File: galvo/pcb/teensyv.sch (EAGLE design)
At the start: 46 parts, among them IC1 RB-0512D, IC10 MCP4922-E/P, IC2.5 MAX6102, IC3 QUAD_OPAMPP, IC5 MAX6105, IC9 QUAD_OPAMPP

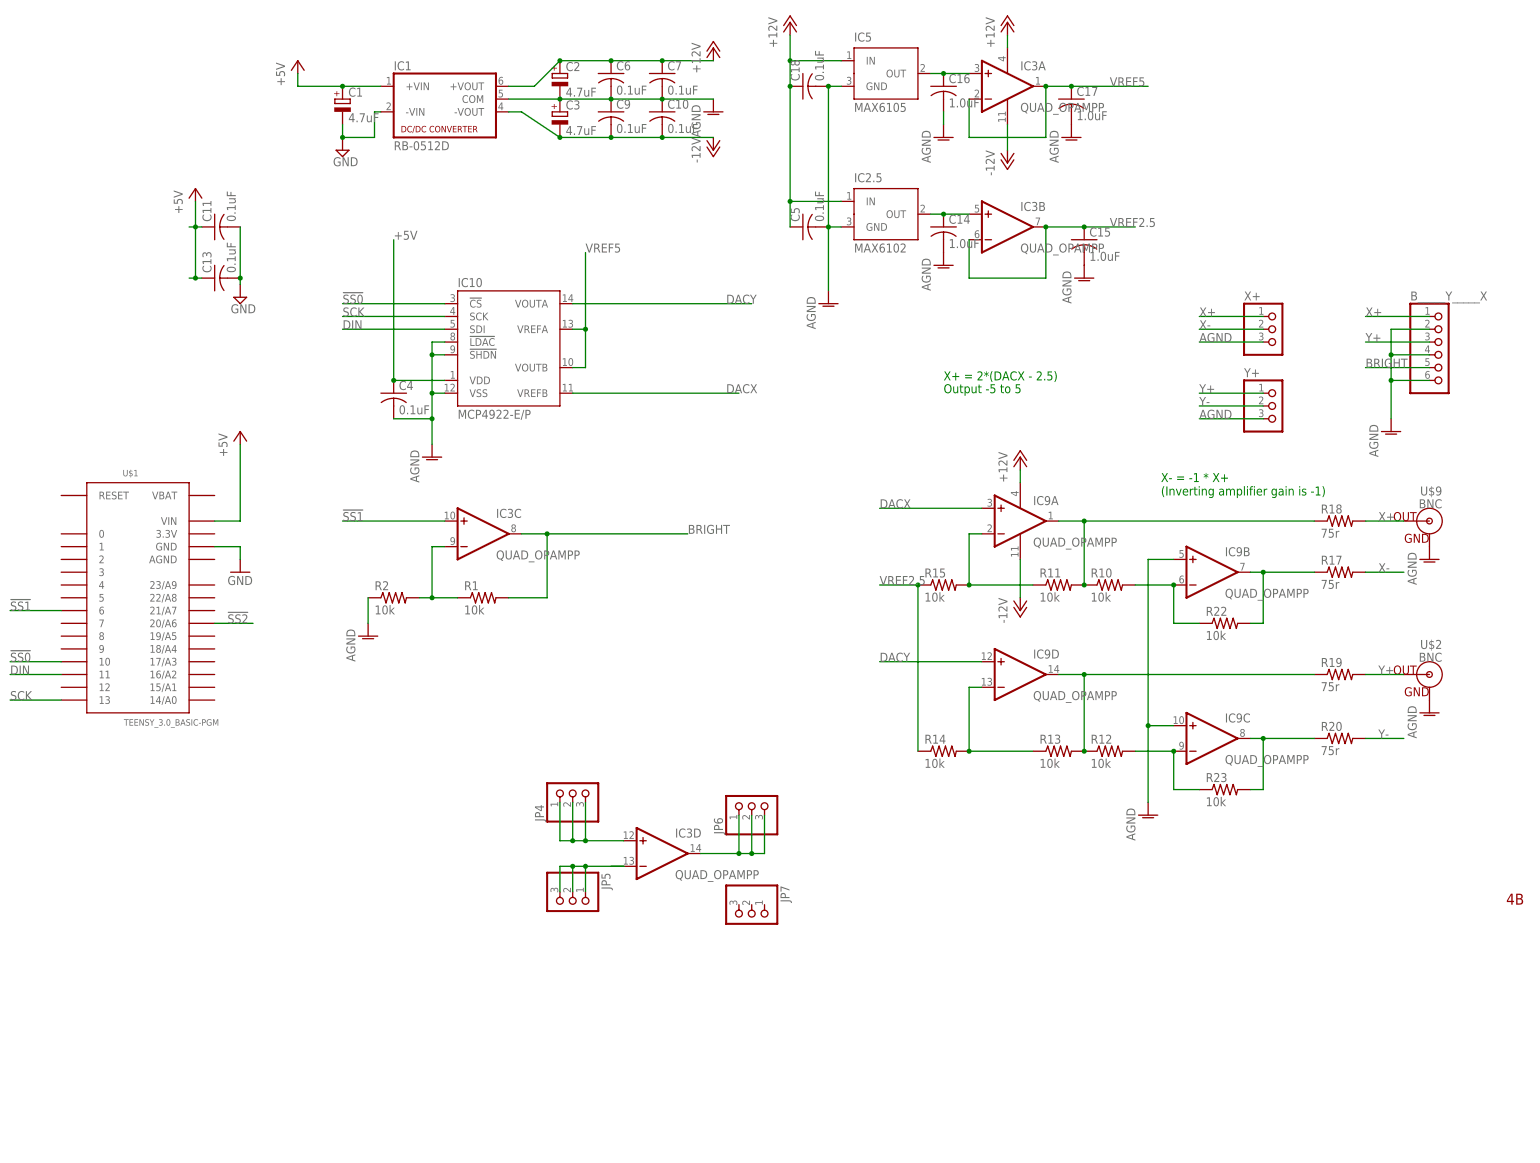
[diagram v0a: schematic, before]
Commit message: added LEDs and extra header
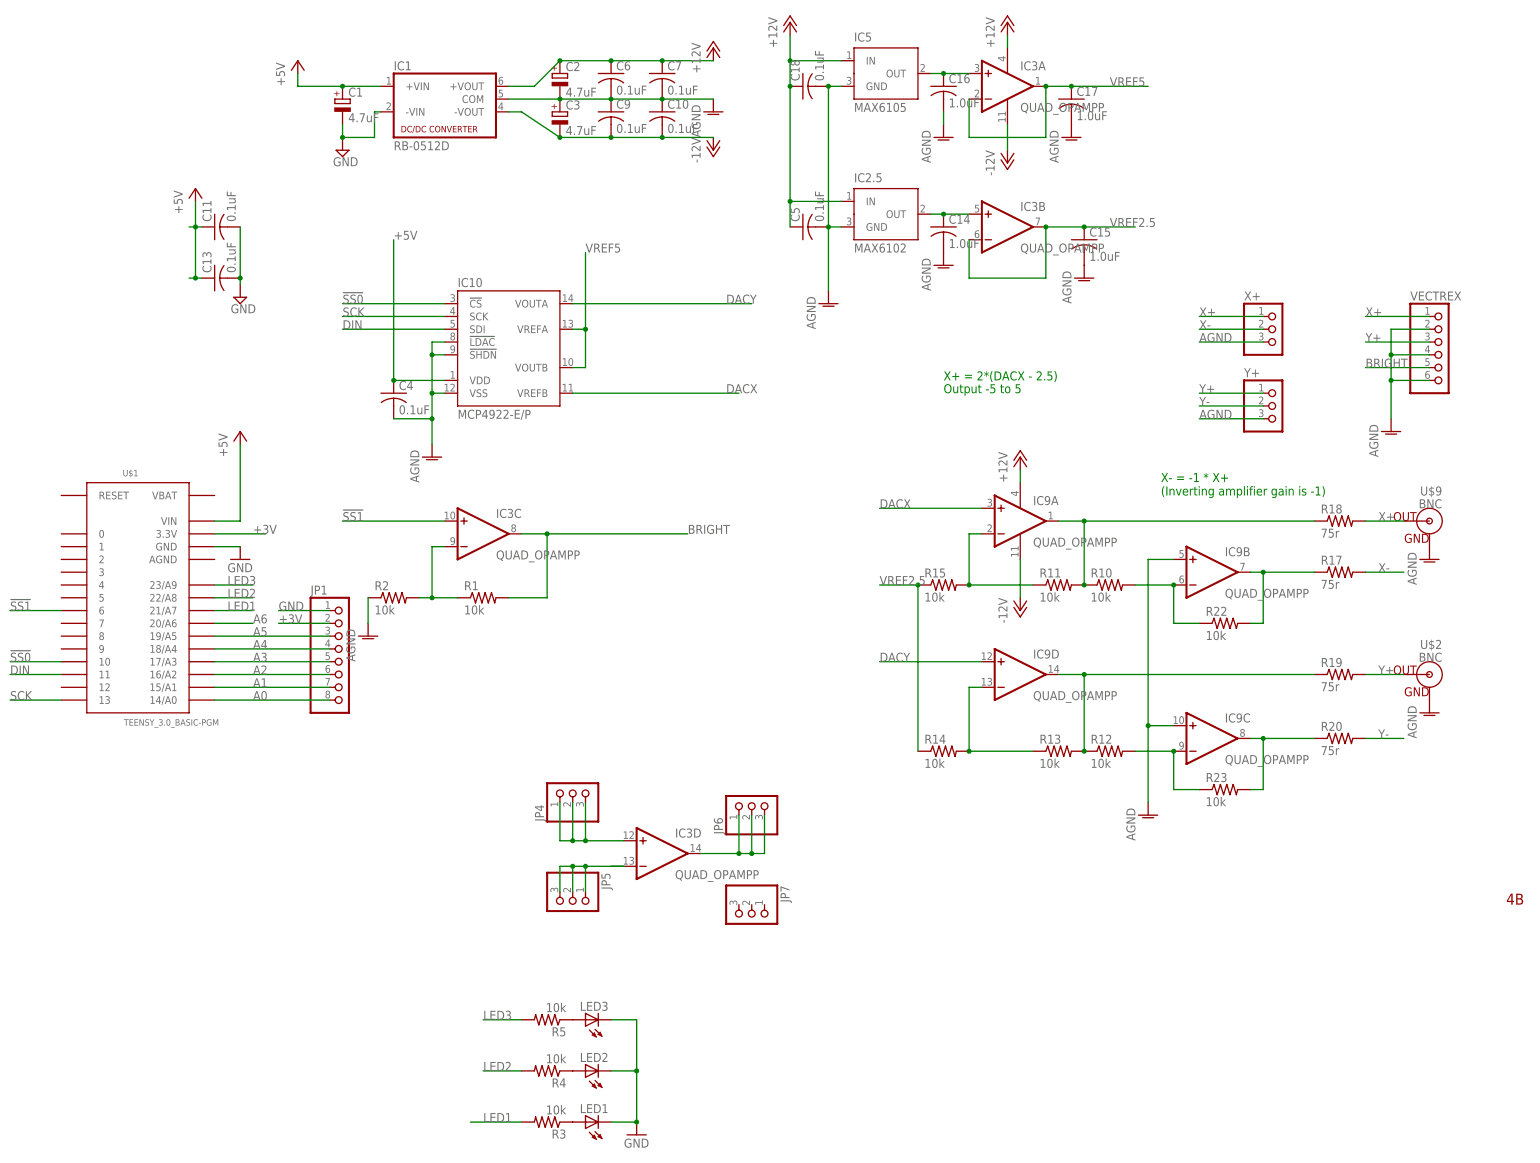
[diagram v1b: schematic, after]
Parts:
- added JP1: (no value), adafruit:PINHD-1X8CLEANBIG
- added LED1, LED2, LED3: (no value), adafruit:LED5MM
- added R3, R4, R5: 10k, adafruit:R-US_0204/2V
- renumbered B_____Y_____X to VECTREX
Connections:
- net !SS2 renamed A6
- new net +3V: JP1.2, U$1.3.3V
- new net A0: JP1.8, U$1.14/A0
- new net A1: JP1.7, U$1.15/A1
- new net A2: JP1.6, U$1.16/A2
- new net A3: JP1.5, U$1.17/A3
- new net A4: JP1.4, U$1.18/A4
- new net A5: JP1.3, U$1.19/A5
- new net LED1: R3.2, U$1.21/A7
- new net LED2: R4.2, U$1.22/A8
- new net LED3: R5.2, U$1.23/A9
- new net N$11: LED2.A, R4.1
- new net N$12: LED3.A, R5.1
- new net N$7: LED1.A, R3.1
- net GND: now also JP1.1, LED1.C, LED2.C, LED3.C
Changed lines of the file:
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@@
 <part name="AGND1" library="supply1" deviceset="AGND" device=""/>
 <part name="AGND2" library="supply1" deviceset="AGND" device=""/>
-<part name="B_____Y_____X" library="adafruit" deviceset="PINHD-1X6" device=""/>
+<part name="VECTREX" library="adafruit" deviceset="PINHD-1X6" device=""/>
 <part name="AGND4" library="supply1" deviceset="AGND" device=""/>
 <part name="X+" library="adafruit" deviceset="PINHD-1X3" device=""/>
@@
 <part name="JP6" library="adafruit" deviceset="PINHD-1X3" device=""/>
 <part name="JP7" library="adafruit" deviceset="PINHD-1X3" device=""/>
+<part name="LED1" library="adafruit" deviceset="LED" device="5MM"/>
+<part name="LED2" library="adafruit" deviceset="LED" device="5MM"/>
+<part name="LED3" library="adafruit" deviceset="LED" device="5MM"/>
+<part name="R3" library="adafruit" deviceset="R-US_" device="0204/2V" value="10k"/>
+<part name="R4" library="adafruit" deviceset="R-US_" device="0204/2V" value="10k"/>
+<part name="R5" library="adafruit" deviceset="R-US_" device="0204/2V" value="10k"/>
+<part name="GND1" library="supply1" deviceset="GND" device=""/>
+<part name="JP1" library="adafruit" deviceset="PINHD-1X8" device="CLEANBIG"/>
 </parts>
 <sheets>
@@
 <instance part="U$1" gate="G$1" x="-33.02" y="68.58"/>
 <instance part="P+2" gate="1" x="-12.7" y="101.6"/>
-<instance part="GND4" gate="1" x="-12.7" y="73.66"/>
+<instance part="GND4" gate="1" x="-12.7" y="76.2"/>
 <instance part="IC3" gate="A" x="139.7" y="170.18"/>
 <instance part="IC3" gate="B" x="139.7" y="142.24"/>
@@
 <instance part="AGND1" gate="VR1" x="223.52" y="76.2"/>
 <instance part="AGND2" gate="VR1" x="223.52" y="45.72"/>
-<instance part="B_____Y_____X" gate="A" x="226.06" y="116.84"/>
+<instance part="VECTREX" gate="A" x="226.06" y="116.84"/>
 <instance part="AGND4" gate="VR1" x="215.9" y="101.6"/>
 <instance part="X+" gate="A" x="193.04" y="121.92"/>
@@
 <instance part="JP6" gate="A" x="88.9" y="27.94" rot="R90"/>
 <instance part="JP7" gate="A" x="88.9" y="5.08" rot="R270"/>
+<instance part="LED1" gate="G$1" x="55.88" y="-35.56" rot="R90"/>
+<instance part="LED2" gate="G$1" x="55.88" y="-25.4" rot="R90"/>
+<instance part="LED3" gate="G$1" x="55.88" y="-15.24" rot="R90"/>
+<instance part="R3" gate="G$1" x="48.26" y="-35.56" rot="R180"/>
+<instance part="R4" gate="G$1" x="48.26" y="-25.4" rot="R180"/>
+<instance part="R5" gate="G$1" x="48.26" y="-15.24" rot="R180"/>
+<instance part="GND1" gate="1" x="66.04" y="-38.1"/>
+<instance part="JP1" gate="G$1" x="7.62" y="58.42"/>
 </instances>
 <busses>
@@
 <pinref part="U$1" gate="G$1" pin="GND"/>
 <wire x1="-17.78" y1="78.74" x2="-12.7" y2="78.74" width="0.1524" layer="91"/>
-<wire x1="-12.7" y1="78.74" x2="-12.7" y2="76.2" width="0.1524" layer="91"/>
 <pinref part="GND4" gate="1" pin="GND"/>
+</segment>
+<segment>
+<pinref part="LED1" gate="G$1" pin="C"/>
+<wire x1="60.96" y1="-35.56" x2="66.04" y2="-35.56" width="0.1524" layer="91"/>
+<wire x1="66.04" y1="-35.56" x2="66.04" y2="-25.4" width="0.1524" layer="91"/>
+<pinref part="LED3" gate="G$1" pin="C"/>
+<wire x1="66.04" y1="-25.4" x2="66.04" y2="-15.24" width="0.1524" layer="91"/>
+<wire x1="66.04" y1="-15.24" x2="60.96" y2="-15.24" width="0.1524" layer="91"/>
+<pinref part="LED2" gate="G$1" pin="C"/>
+<wire x1="60.96" y1="-25.4" x2="66.04" y2="-25.4" width="0.1524" layer="91"/>
+<junction x="66.04" y="-25.4"/>
+<pinref part="GND1" gate="1" pin="GND"/>
+<junction x="66.04" y="-35.56"/>
+</segment>
+<segment>
+<pinref part="JP1" gate="G$1" pin="1"/>
+<wire x1="5.08" y1="66.04" x2="-5.08" y2="66.04" width="0.1524" layer="91"/>
+<label x="-5.08" y="66.04" size="1.778" layer="95"/>
 </segment>
 </net>
@@
 </segment>
 <segment>
-<pinref part="B_____Y_____X" gate="A" pin="1"/>
+<pinref part="VECTREX" gate="A" pin="1"/>
 <wire x1="223.52" y1="124.46" x2="210.82" y2="124.46" width="0.1524" layer="91"/>
 <label x="210.82" y="124.46" size="1.778" layer="95"/>
@@
 </segment>
 <segment>
-<pinref part="B_____Y_____X" gate="A" pin="3"/>
+<pinref part="VECTREX" gate="A" pin="3"/>
 <wire x1="223.52" y1="119.38" x2="210.82" y2="119.38" width="0.1524" layer="91"/>
 <label x="210.82" y="119.38" size="1.778" layer="95"/>
@@
 </segment>
 </net>
-<net name="!SS2" class="0">
+<net name="A6" class="0">
 <segment>
 <pinref part="U$1" gate="G$1" pin="20/A6"/>
 <wire x1="-17.78" y1="63.5" x2="-10.16" y2="63.5" width="0.1524" layer="91"/>
-<label x="-15.24" y="63.5" size="1.778" layer="95"/>
+<label x="-10.16" y="63.5" size="1.778" layer="95"/>
 </segment>
 </net>
@@
 </segment>
 <segment>
-<pinref part="B_____Y_____X" gate="A" pin="5"/>
+<pinref part="VECTREX" gate="A" pin="5"/>
 <wire x1="223.52" y1="114.3" x2="210.82" y2="114.3" width="0.1524" layer="91"/>
 <label x="210.82" y="114.3" size="1.778" layer="95"/>
@@
 </segment>
 <segment>
-<pinref part="B_____Y_____X" gate="A" pin="4"/>
+<pinref part="VECTREX" gate="A" pin="4"/>
 <wire x1="223.52" y1="116.84" x2="215.9" y2="116.84" width="0.1524" layer="91"/>
 <wire x1="215.9" y1="116.84" x2="215.9" y2="111.76" width="0.1524" layer="91"/>
-<pinref part="B_____Y_____X" gate="A" pin="6"/>
+<pinref part="VECTREX" gate="A" pin="6"/>
 <wire x1="215.9" y1="111.76" x2="215.9" y2="104.14" width="0.1524" layer="91"/>
 <wire x1="223.52" y1="111.76" x2="215.9" y2="111.76" width="0.1524" layer="91"/>
-<pinref part="B_____Y_____X" gate="A" pin="2"/>
+<pinref part="VECTREX" gate="A" pin="2"/>
 <wire x1="223.52" y1="121.92" x2="215.9" y2="121.92" width="0.1524" layer="91"/>
 <wire x1="215.9" y1="121.92" x2="215.9" y2="116.84" width="0.1524" layer="91"/>
@@
 </segment>
 </net>
+<net name="N$7" class="0">
+<segment>
+<pinref part="LED1" gate="G$1" pin="A"/>
+<pinref part="R3" gate="G$1" pin="1"/>
+</segment>
+</net>
+<net name="N$11" class="0">
+<segment>
+<pinref part="LED2" gate="G$1" pin="A"/>
+<pinref part="R4" gate="G$1" pin="1"/>
+</segment>
+</net>
+<net name="N$12" class="0">
+<segment>
+<pinref part="LED3" gate="G$1" pin="A"/>
+<pinref part="R5" gate="G$1" pin="1"/>
+</segment>
+</net>
+<net name="LED3" class="0">
+<segment>
+<pinref part="R5" gate="G$1" pin="2"/>
+<wire x1="43.18" y1="-15.24" x2="35.56" y2="-15.24" width="0.1524" layer="91"/>
+<label x="35.56" y="-15.24" size="1.778" layer="95"/>
+</segment>
+<segment>
+<pinref part="U$1" gate="G$1" pin="23/A9"/>
+<wire x1="-17.78" y1="71.12" x2="-10.16" y2="71.12" width="0.1524" layer="91"/>
+<label x="-15.24" y="71.12" size="1.778" layer="95"/>
+</segment>
+</net>
+<net name="LED2" class="0">
+<segment>
+<pinref part="R4" gate="G$1" pin="2"/>
+<wire x1="43.18" y1="-25.4" x2="35.56" y2="-25.4" width="0.1524" layer="91"/>
+<label x="35.56" y="-25.4" size="1.778" layer="95"/>
+</segment>
+<segment>
+<pinref part="U$1" gate="G$1" pin="22/A8"/>
+<wire x1="-17.78" y1="68.58" x2="-10.16" y2="68.58" width="0.1524" layer="91"/>
+<label x="-15.24" y="68.58" size="1.778" layer="95"/>
+</segment>
+</net>
+<net name="LED1" class="0">
+<segment>
+<pinref part="R3" gate="G$1" pin="2"/>
+<wire x1="43.18" y1="-35.56" x2="33.02" y2="-35.56" width="0.1524" layer="91"/>
+<label x="35.56" y="-35.56" size="1.778" layer="95"/>
+</segment>
+<segment>
+<pinref part="U$1" gate="G$1" pin="21/A7"/>
+<wire x1="-17.78" y1="66.04" x2="-10.16" y2="66.04" width="0.1524" layer="91"/>
+<label x="-15.24" y="66.04" size="1.778" layer="95"/>
+</segment>
+</net>
+<net name="A0" class="0">
+<segment>
+<pinref part="U$1" gate="G$1" pin="14/A0"/>
+<wire x1="-17.78" y1="48.26" x2="5.08" y2="48.26" width="0.1524" layer="91"/>
+<label x="-10.16" y="48.26" size="1.778" layer="95"/>
+<pinref part="JP1" gate="G$1" pin="8"/>
+</segment>
+</net>
+<net name="A1" class="0">
+<segment>
+<pinref part="U$1" gate="G$1" pin="15/A1"/>
+<wire x1="-17.78" y1="50.8" x2="5.08" y2="50.8" width="0.1524" layer="91"/>
+<label x="-10.16" y="50.8" size="1.778" layer="95"/>
+<pinref part="JP1" gate="G$1" pin="7"/>
+</segment>
+</net>
+<net name="A2" class="0">
+<segment>
+<pinref part="U$1" gate="G$1" pin="16/A2"/>
+<wire x1="-17.78" y1="53.34" x2="5.08" y2="53.34" width="0.1524" layer="91"/>
+<label x="-10.16" y="53.34" size="1.778" layer="95"/>
+<pinref part="JP1" gate="G$1" pin="6"/>
+</segment>
+</net>
+<net name="A3" class="0">
+<segment>
+<pinref part="U$1" gate="G$1" pin="17/A3"/>
+<wire x1="-17.78" y1="55.88" x2="5.08" y2="55.88" width="0.1524" layer="91"/>
+<label x="-10.16" y="55.88" size="1.778" layer="95"/>
+<pinref part="JP1" gate="G$1" pin="5"/>
+</segment>
+</net>
+<net name="A4" class="0">
+<segment>
+<pinref part="U$1" gate="G$1" pin="18/A4"/>
+<wire x1="-17.78" y1="58.42" x2="5.08" y2="58.42" width="0.1524" layer="91"/>
+<label x="-10.16" y="58.42" size="1.778" layer="95"/>
+<pinref part="JP1" gate="G$1" pin="4"/>
+</segment>
+</net>
+<net name="A5" class="0">
+<segment>
+<pinref part="U$1" gate="G$1" pin="19/A5"/>
+<wire x1="-17.78" y1="60.96" x2="5.08" y2="60.96" width="0.1524" layer="91"/>
+<label x="-10.16" y="60.96" size="1.778" layer="95"/>
+<pinref part="JP1" gate="G$1" pin="3"/>
+</segment>
+</net>
+<net name="+3V" class="0">
+<segment>
+<pinref part="JP1" gate="G$1" pin="2"/>
+<wire x1="5.08" y1="63.5" x2="-5.08" y2="63.5" width="0.1524" layer="91"/>
+<label x="-5.08" y="63.5" size="1.778" layer="95"/>
+</segment>
+<segment>
+<pinref part="U$1" gate="G$1" pin="3.3V"/>
+<wire x1="-17.78" y1="81.28" x2="-7.62" y2="81.28" width="0.1524" layer="91"/>
+<label x="-10.16" y="81.28" size="1.778" layer="95"/>
+</segment>
+</net>
